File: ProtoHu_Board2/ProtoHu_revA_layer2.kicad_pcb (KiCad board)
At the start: 2 copper layers, 54 x 85.6 mm, 0 parts

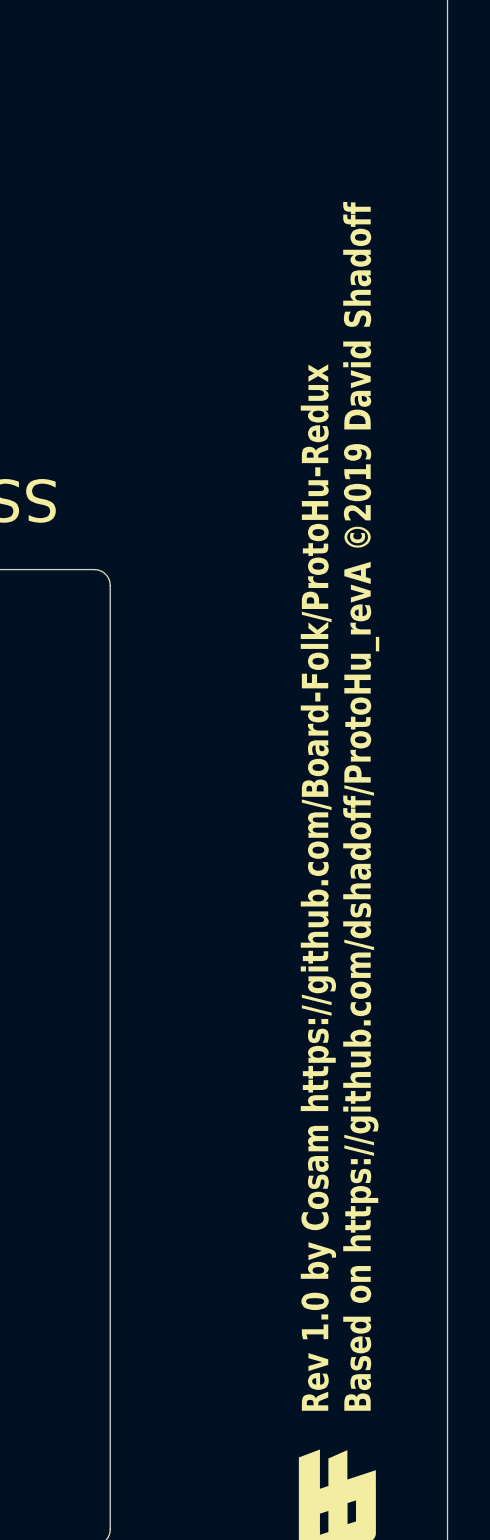
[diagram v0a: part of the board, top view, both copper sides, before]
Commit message: Correct Board 1 thickness hint on silkscreen.
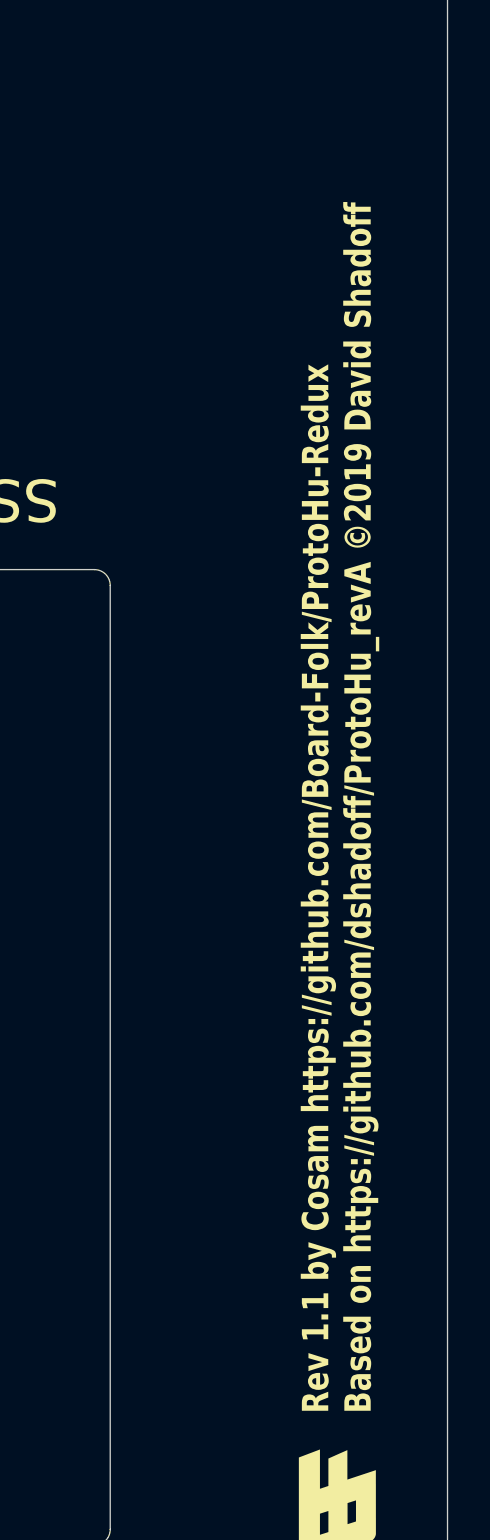
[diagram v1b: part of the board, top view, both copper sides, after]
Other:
- board text added: "Rev 1.1 by Cosam https://github.com/Board-Folk/ProtoHu-Redux Based on https://github.com/dshadoff/ProtoHu_revA ©2019 David Shadoff"
- board text removed: "Rev 1.0 by Cosam https://github.com/Board-Folk/ProtoHu-Redux Based on https://github.com/dshadoff/ProtoHu_revA ©2019 David Shadoff"
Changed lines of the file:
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@@
     (effects (font (size 2 2) (thickness 0.2)) (justify bottom))
   )
-  (gr_text "Rev 1.0 by Cosam https://github.com/Board-Folk/ProtoHu-Redux\nBased on https://github.com/dshadoff/ProtoHu_revA ©2019 David Shadoff" (at 172 137 90) (layer "F.SilkS")
+  (gr_text "Rev 1.1 by Cosam https://github.com/Board-Folk/ProtoHu-Redux\nBased on https://github.com/dshadoff/ProtoHu_revA ©2019 David Shadoff" (at 172 137 90) (layer "F.SilkS")
     (effects (font (size 1.25 1) (thickness 0.15) bold) (justify left bottom))
   )
